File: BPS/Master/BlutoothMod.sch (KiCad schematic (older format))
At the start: 4 parts

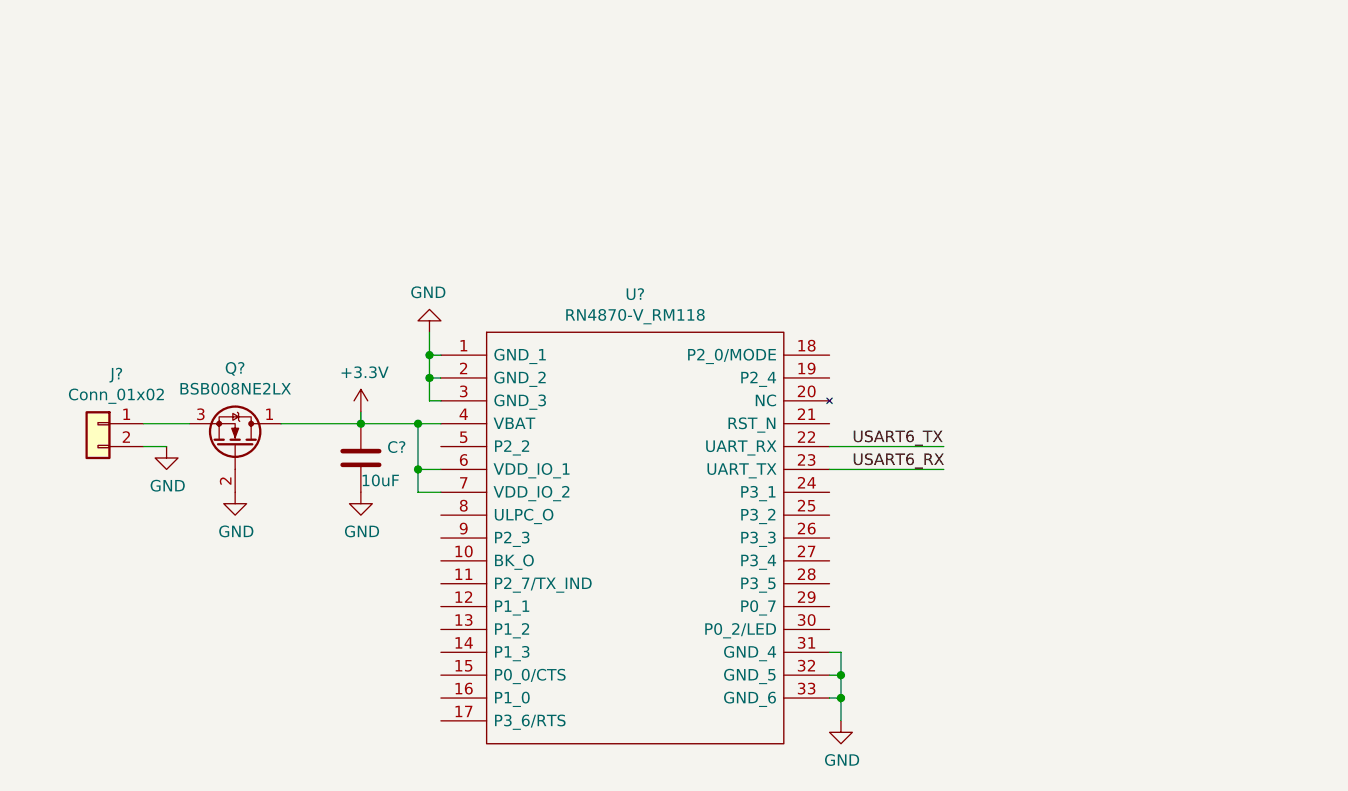
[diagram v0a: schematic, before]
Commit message: Added annotations to all schematic symbols. Ran electrical rules check. Need to figure out how to connect pins between sheets. Added reset circuit and finished reverse voltage protection circuit. Need to add configuration interface after finding out which pins to use on STM.
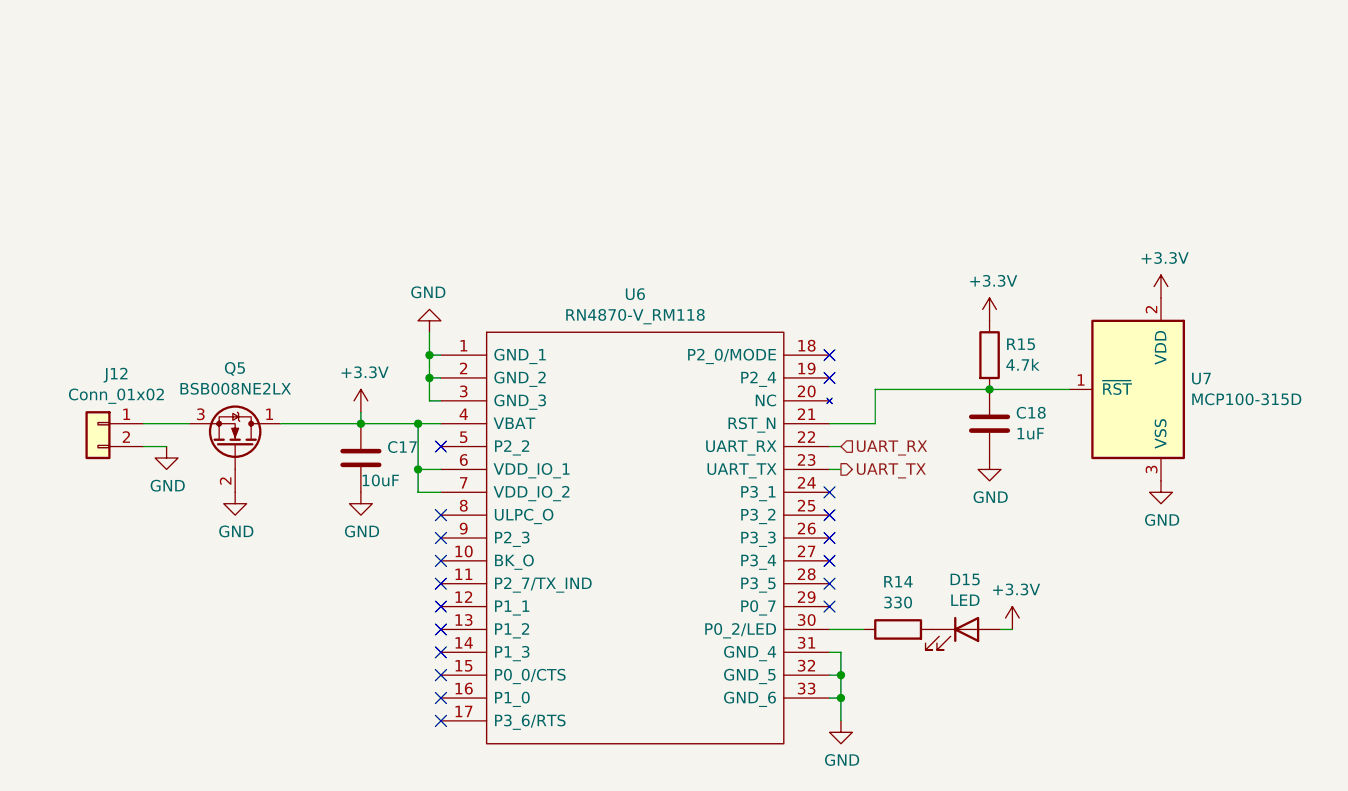
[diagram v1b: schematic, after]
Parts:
- added C18: 1uF, symbol Device:C
- added D15: LED, symbol Device:LED
- added R14: 330, symbol Device:R
- added R15: 4.7k, symbol Device:R
- added U7: MCP100-315D, symbol Power_Supervisor:MCP100-315D
- gave numbers to parts that had none: 4
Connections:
- net labels added: UART_RX, UART_TX
- net labels removed: USART6_RX, USART6_TX
- wire segments 24 -> 30
- no-connect marks 0 -> 19
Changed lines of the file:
@@
 $EndDescr
 $Comp
-L utsvt-bltmod:RN4870-V_RM118 U?
+L utsvt-bltmod:RN4870-V_RM118 U6
 U 1 1 5EE47912
 P 5000 2900
-F 0 "U?" H 5850 3165 50  0000 C CNN
+F 0 "U6" H 5850 3165 50  0000 C CNN
 F 1 "RN4870-V_RM118" H 5850 3074 50  0000 C CNN
 F 2 "RN4870IRM130" H 6550 3000 50  0001 L CNN
@@
 	1    0    0    -1
 $EndComp
-Text Label 6800 3300 0    50   ~ 0
-USART6_TX
-Wire Wire Line
-	6700 3300 7200 3300
-Wire Wire Line
-	6700 3400 7200 3400
-Text Label 6800 3400 0    50   ~ 0
-USART6_RX
 Wire Wire Line
 	6700 4200 6750 4200
@@
 Connection ~ 6750 4400
 $Comp
-L power:GND #PWR?
+L power:GND #PWR0106
 U 1 1 5EE48E9A
 P 6750 4500
-F 0 "#PWR?" H 6750 4250 50  0001 C CNN
+F 0 "#PWR0106" H 6750 4250 50  0001 C CNN
 F 1 "GND" H 6755 4327 50  0000 C CNN
 F 2 "" H 6750 4500 50  0001 C CNN
@@
 Connection ~ 4950 2900
 $Comp
-L power:GND #PWR?
+L power:GND #PWR0107
 U 1 1 5EE4937A
 P 4950 2800
-F 0 "#PWR?" H 4950 2550 50  0001 C CNN
+F 0 "#PWR0107" H 4950 2550 50  0001 C CNN
 F 1 "GND" H 4955 2627 50  0000 C CNN
 F 2 "" H 4950 2800 50  0001 C CNN
@@
 Connection ~ 4900 3200
 $Comp
-L power:GND #PWR?
+L power:GND #PWR0108
 U 1 1 5EE4ABF0
 P 4650 3500
-F 0 "#PWR?" H 4650 3250 50  0001 C CNN
+F 0 "#PWR0108" H 4650 3250 50  0001 C CNN
 F 1 "GND" H 4655 3327 50  0000 C CNN
 F 2 "" H 4650 3500 50  0001 C CNN
@@
 $EndComp
 $Comp
-L power:+3.3V #PWR?
+L power:+3.3V #PWR0109
 U 1 1 5EE4AD11
 P 4650 3150
-F 0 "#PWR?" H 4650 3000 50  0001 C CNN
+F 0 "#PWR0109" H 4650 3000 50  0001 C CNN
 F 1 "+3.3V" H 4665 3323 50  0000 C CNN
 F 2 "" H 4650 3150 50  0001 C CNN
@@
 $EndComp
 $Comp
-L Device:C C?
+L Device:C C17
 U 1 1 5EE4B59B
 P 4650 3350
-F 0 "C?" H 4765 3396 50  0000 L CNN
+F 0 "C17" H 4765 3396 50  0000 L CNN
 F 1 "10uF" H 4650 3250 50  0000 L CNN
 F 2 "" H 4688 3200 50  0001 C CNN
@@
 	4650 3200 4300 3200
 $Comp
-L Transistor_FET:BSB008NE2LX Q?
+L Transistor_FET:BSB008NE2LX Q5
 U 1 1 5EE62400
 P 4100 3300
-F 0 "Q?" V 4442 3300 50  0000 C CNN
+F 0 "Q5" V 4442 3300 50  0000 C CNN
 F 1 "BSB008NE2LX" V 4351 3300 50  0000 C CNN
 F 2 "Package_DirectFET:DirectFET_MX" H 4100 3300 50  0001 C CIN
@@
 $EndComp
 $Comp
-L power:GND #PWR?
+L power:GND #PWR0110
 U 1 1 5EE6457A
 P 4100 3500
-F 0 "#PWR?" H 4100 3250 50  0001 C CNN
+F 0 "#PWR0110" H 4100 3250 50  0001 C CNN
 F 1 "GND" H 4105 3327 50  0000 C CNN
 F 2 "" H 4100 3500 50  0001 C CNN
@@
 $EndComp
 $Comp
-L Connector_Generic:Conn_01x02 J?
+L Connector_Generic:Conn_01x02 J12
 U 1 1 5EE69056
 P 3500 3200
-F 0 "J?" H 3418 3417 50  0000 C CNN
+F 0 "J12" H 3418 3417 50  0000 C CNN
 F 1 "Conn_01x02" H 3418 3326 50  0000 C CNN
 F 2 "" H 3500 3200 50  0001 C CNN
@@
 	3700 3300 3800 3300
 $Comp
-L power:GND #PWR?
+L power:GND #PWR0111
 U 1 1 5EE6AECF
 P 3800 3300
-F 0 "#PWR?" H 3800 3050 50  0001 C CNN
+F 0 "#PWR0111" H 3800 3050 50  0001 C CNN
 F 1 "GND" H 3805 3127 50  0000 C CNN
 F 2 "" H 3800 3300 50  0001 C CNN
@@
 	1    0    0    -1
 $EndComp
+Wire Wire Line
+	6700 3200 6900 3200
+Wire Wire Line
+	6900 3200 6900 3050
+$Comp
+L Power_Supervisor:MCP100-315D U7
+U 1 1 5EE0F520
+P 8050 3050
+F 0 "U7" H 7820 3096 50  0000 R CNN
+F 1 "MCP100-315D" H 7820 3005 50  0000 R CNN
+F 2 "" H 7650 3200 50  0001 C CNN
+F 3 "http://ww1.microchip.com/downloads/en/DeviceDoc/11187f.pdf" H 7750 3300 50  0001 C CNN
+	1    8050 3050
+	-1   0    0    -1
+$EndComp
+Wire Wire Line
+	6900 3050 7400 3050
+$Comp
+L power:+3.3V #PWR0112
+U 1 1 5EE112CA
+P 7400 2750
+F 0 "#PWR0112" H 7400 2600 50  0001 C CNN
+F 1 "+3.3V" H 7415 2923 50  0000 C CNN
+F 2 "" H 7400 2750 50  0001 C CNN
+F 3 "" H 7400 2750 50  0001 C CNN
+	1    7400 2750
+	1    0    0    -1
+$EndComp
+$Comp
+L Device:R R15
+U 1 1 5EE108D1
+P 7400 2900
+F 0 "R15" H 7470 2946 50  0000 L CNN
+F 1 "4.7k" H 7470 2855 50  0000 L CNN
+F 2 "" V 7330 2900 50  0001 C CNN
+F 3 "~" H 7400 2900 50  0001 C CNN
+	1    7400 2900
+	1    0    0    -1
+$EndComp
+$Comp
+L Device:C C18
+U 1 1 5EE11D9D
+P 7400 3200
+F 0 "C18" H 7515 3246 50  0000 L CNN
+F 1 "1uF" H 7515 3155 50  0000 L CNN
+F 2 "" H 7438 3050 50  0001 C CNN
+F 3 "~" H 7400 3200 50  0001 C CNN
+	1    7400 3200
+	1    0    0    -1
+$EndComp
+Connection ~ 7400 3050
+$Comp
+L power:GND #PWR0113
+U 1 1 5EE12187
+P 7400 3350
+F 0 "#PWR0113" H 7400 3100 50  0001 C CNN
+F 1 "GND" H 7405 3177 50  0000 C CNN
+F 2 "" H 7400 3350 50  0001 C CNN
+F 3 "" H 7400 3350 50  0001 C CNN
+	1    7400 3350
+	1    0    0    -1
+$EndComp
+Wire Wire Line
+	7400 3050 7750 3050
+$Comp
+L power:GND #PWR0114
+U 1 1 5EE1353A
+P 8150 3450
+F 0 "#PWR0114" H 8150 3200 50  0001 C CNN
+F 1 "GND" H 8155 3277 50  0000 C CNN
+F 2 "" H 8150 3450 50  0001 C CNN
+F 3 "" H 8150 3450 50  0001 C CNN
+	1    8150 3450
+	1    0    0    -1
+$EndComp
+$Comp
+L power:+3.3V #PWR0115
+U 1 1 5EE13791
+P 8150 2650
+F 0 "#PWR0115" H 8150 2500 50  0001 C CNN
+F 1 "+3.3V" H 8165 2823 50  0000 C CNN
+F 2 "" H 8150 2650 50  0001 C CNN
+F 3 "" H 8150 2650 50  0001 C CNN
+	1    8150 2650
+	1    0    0    -1
+$EndComp
+$Comp
+L Device:R R14
+U 1 1 5EE13A0C
+P 7000 4100
+F 0 "R14" V 7207 4100 50  0000 C CNN
+F 1 "330" V 7116 4100 50  0000 C CNN
+F 2 "" V 6930 4100 50  0001 C CNN
+F 3 "~" H 7000 4100 50  0001 C CNN
+	1    7000 4100
+	0    -1   -1   0
+$EndComp
+Wire Wire Line
+	6700 4100 6850 4100
+$Comp
+L Device:LED D15
+U 1 1 5EE14D8D
+P 7300 4100
+F 0 "D15" H 7293 4317 50  0000 C CNN
+F 1 "LED" H 7293 4226 50  0000 C CNN
+F 2 "" H 7300 4100 50  0001 C CNN
+F 3 "~" H 7300 4100 50  0001 C CNN
+	1    7300 4100
+	1    0    0    -1
+$EndComp
+$Comp
+L power:+3.3V #PWR0116
+U 1 1 5EE14FBF
+P 7500 4100
+F 0 "#PWR0116" H 7500 3950 50  0001 C CNN
+F 1 "+3.3V" H 7515 4273 50  0000 C CNN
+F 2 "" H 7500 4100 50  0001 C CNN
+F 3 "" H 7500 4100 50  0001 C CNN
+	1    7500 4100
+	1    0    0    -1
+$EndComp
+Wire Wire Line
+	7450 4100 7500 4100
+NoConn ~ 6700 2900
+NoConn ~ 6700 3000
+NoConn ~ 6700 3500
+NoConn ~ 6700 3600
+NoConn ~ 6700 3700
+NoConn ~ 6700 3800
+NoConn ~ 6700 3900
+NoConn ~ 6700 4000
+NoConn ~ 5000 4500
+NoConn ~ 5000 4400
+NoConn ~ 5000 4300
+NoConn ~ 5000 4200
+NoConn ~ 5000 4100
+NoConn ~ 5000 4000
+NoConn ~ 5000 3900
+NoConn ~ 5000 3800
+NoConn ~ 5000 3700
+NoConn ~ 5000 3600
+NoConn ~ 5000 3300
+Text HLabel 6750 3300 2    50   Input ~ 0
+UART_RX
+Text HLabel 6750 3400 2    50   Output ~ 0
+UART_TX
+Wire Wire Line
+	6700 3300 6750 3300
+Wire Wire Line
+	6700 3400 6750 3400
 $EndSCHEMATC

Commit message: Connected hierarchial sheets. Added text for all status led's.
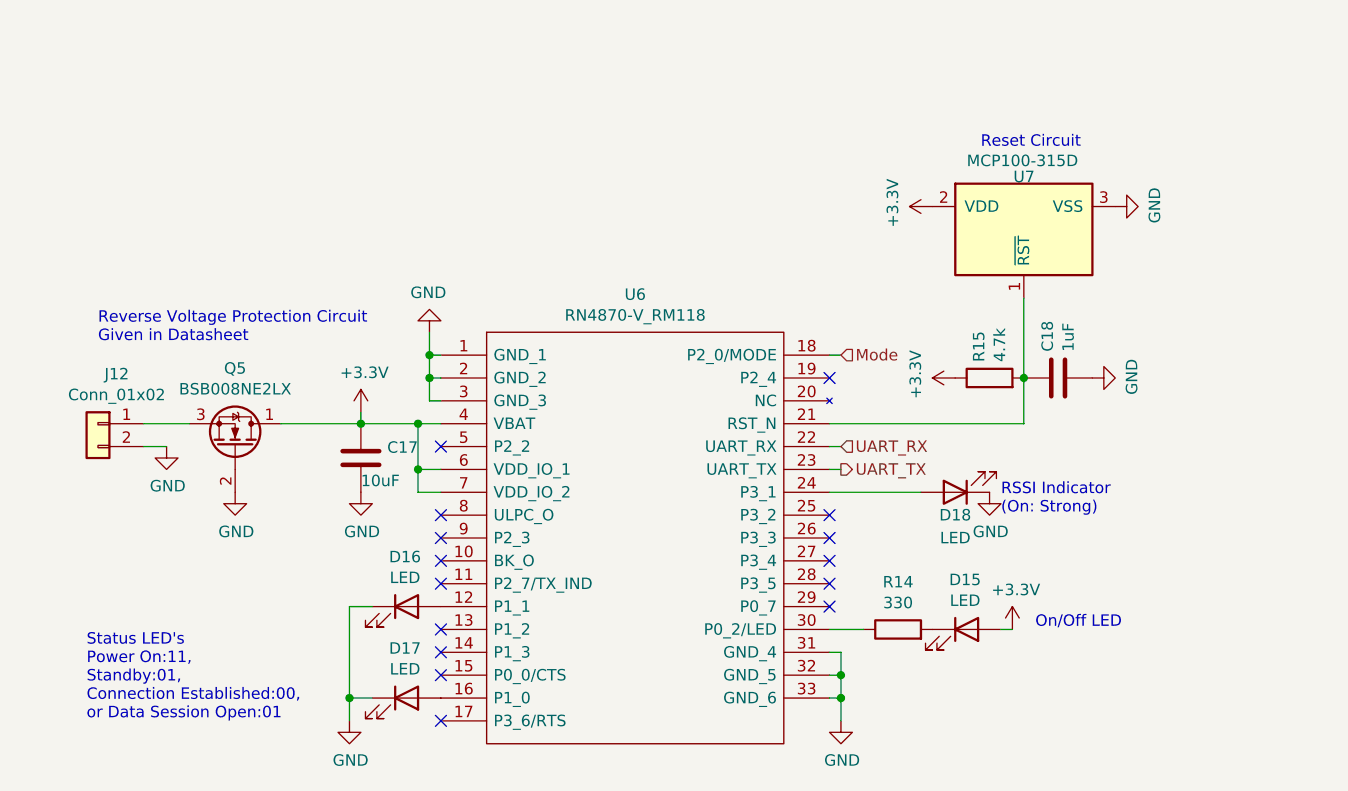
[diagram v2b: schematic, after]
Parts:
- added D16, D17, D18: LED, symbol Device:LED
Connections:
- net GND: now also D16.1 (K), D17.1 (K), D18.1 (K)
- net at U6.12 (P1_1): now also D16.2 (A)
- net at U6.16 (P1_0): now also D17.2 (A)
- net Mode: now reaches U6.18 (P2_0/MODE)
- net at U6.24 (P3_1): now also D18.2 (A)
- no-connect marks 19 -> 15
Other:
- note added: "On/Off LED"
- note added: "RSSI Indicator\n(On: Strong)"
- note added: "Reset Circuit\n"
- note added: "Reverse Voltage Protection Circuit\nGiven in Datasheet"
- note added: "Status LED's\nPower On:11,\nStandby:01,\nConnection Established:00,\nor Data Session Open:01"
- moved on the sheet: C18, R15, U7
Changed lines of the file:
@@
 	1    0    0    -1
 $EndComp
-Wire Wire Line
-	6700 3200 6900 3200
-Wire Wire Line
-	6900 3200 6900 3050
-$Comp
-L Power_Supervisor:MCP100-315D U7
-U 1 1 5EE0F520
-P 8050 3050
-F 0 "U7" H 7820 3096 50  0000 R CNN
-F 1 "MCP100-315D" H 7820 3005 50  0000 R CNN
-F 2 "" H 7650 3200 50  0001 C CNN
-F 3 "http://ww1.microchip.com/downloads/en/DeviceDoc/11187f.pdf" H 7750 3300 50  0001 C CNN
-	1    8050 3050
-	-1   0    0    -1
-$EndComp
-Wire Wire Line
-	6900 3050 7400 3050
 $Comp
 L power:+3.3V #PWR0112
 U 1 1 5EE112CA
-P 7400 2750
-F 0 "#PWR0112" H 7400 2600 50  0001 C CNN
-F 1 "+3.3V" H 7415 2923 50  0000 C CNN
-F 2 "" H 7400 2750 50  0001 C CNN
-F 3 "" H 7400 2750 50  0001 C CNN
-	1    7400 2750
-	1    0    0    -1
+P 7250 3000
+F 0 "#PWR0112" H 7250 2850 50  0001 C CNN
+F 1 "+3.3V" H 7265 3173 50  0000 C CNN
+F 2 "" H 7250 3000 50  0001 C CNN
+F 3 "" H 7250 3000 50  0001 C CNN
+	1    7250 3000
+	0    -1   -1   0
 $EndComp
 $Comp
 L Device:R R15
 U 1 1 5EE108D1
-P 7400 2900
-F 0 "R15" H 7470 2946 50  0000 L CNN
-F 1 "4.7k" H 7470 2855 50  0000 L CNN
-F 2 "" V 7330 2900 50  0001 C CNN
-F 3 "~" H 7400 2900 50  0001 C CNN
-	1    7400 2900
-	1    0    0    -1
+P 7400 3000
+F 0 "R15" H 7470 3046 50  0000 L CNN
+F 1 "4.7k" H 7470 2955 50  0000 L CNN
+F 2 "" V 7330 3000 50  0001 C CNN
+F 3 "~" H 7400 3000 50  0001 C CNN
+	1    7400 3000
+	0    -1   -1   0
 $EndComp
 $Comp
 L Device:C C18
 U 1 1 5EE11D9D
-P 7400 3200
-F 0 "C18" H 7515 3246 50  0000 L CNN
-F 1 "1uF" H 7515 3155 50  0000 L CNN
-F 2 "" H 7438 3050 50  0001 C CNN
-F 3 "~" H 7400 3200 50  0001 C CNN
-	1    7400 3200
-	1    0    0    -1
-$EndComp
-Connection ~ 7400 3050
+P 7700 3000
+F 0 "C18" H 7815 3046 50  0000 L CNN
+F 1 "1uF" H 7815 2955 50  0000 L CNN
+F 2 "" H 7738 2850 50  0001 C CNN
+F 3 "~" H 7700 3000 50  0001 C CNN
+	1    7700 3000
+	0    -1   -1   0
+$EndComp
+Connection ~ 7550 3000
 $Comp
 L power:GND #PWR0113
 U 1 1 5EE12187
-P 7400 3350
-F 0 "#PWR0113" H 7400 3100 50  0001 C CNN
-F 1 "GND" H 7405 3177 50  0000 C CNN
-F 2 "" H 7400 3350 50  0001 C CNN
-F 3 "" H 7400 3350 50  0001 C CNN
-	1    7400 3350
-	1    0    0    -1
-$EndComp
-Wire Wire Line
-	7400 3050 7750 3050
+P 7850 3000
+F 0 "#PWR0113" H 7850 2750 50  0001 C CNN
+F 1 "GND" H 7855 2827 50  0000 C CNN
+F 2 "" H 7850 3000 50  0001 C CNN
+F 3 "" H 7850 3000 50  0001 C CNN
+	1    7850 3000
+	0    -1   -1   0
+$EndComp
+Wire Wire Line
+	7550 3000 7550 2650
 $Comp
 L power:GND #PWR0114
 U 1 1 5EE1353A
-P 8150 3450
-F 0 "#PWR0114" H 8150 3200 50  0001 C CNN
-F 1 "GND" H 8155 3277 50  0000 C CNN
-F 2 "" H 8150 3450 50  0001 C CNN
-F 3 "" H 8150 3450 50  0001 C CNN
-	1    8150 3450
-	1    0    0    -1
+P 7950 2250
+F 0 "#PWR0114" H 7950 2000 50  0001 C CNN
+F 1 "GND" H 7955 2077 50  0000 C CNN
+F 2 "" H 7950 2250 50  0001 C CNN
+F 3 "" H 7950 2250 50  0001 C CNN
+	1    7950 2250
+	0    -1   -1   0
 $EndComp
 $Comp
 L power:+3.3V #PWR0115
 U 1 1 5EE13791
-P 8150 2650
-F 0 "#PWR0115" H 8150 2500 50  0001 C CNN
-F 1 "+3.3V" H 8165 2823 50  0000 C CNN
-F 2 "" H 8150 2650 50  0001 C CNN
-F 3 "" H 8150 2650 50  0001 C CNN
-	1    8150 2650
-	1    0    0    -1
+P 7150 2250
+F 0 "#PWR0115" H 7150 2100 50  0001 C CNN
+F 1 "+3.3V" H 7165 2423 50  0000 C CNN
+F 2 "" H 7150 2250 50  0001 C CNN
+F 3 "" H 7150 2250 50  0001 C CNN
+	1    7150 2250
+	0    -1   -1   0
 $EndComp
 $Comp
@@
 Wire Wire Line
 	7450 4100 7500 4100
-NoConn ~ 6700 2900
 NoConn ~ 6700 3000
-NoConn ~ 6700 3500
 NoConn ~ 6700 3600
 NoConn ~ 6700 3700
@@
 NoConn ~ 6700 4000
 NoConn ~ 5000 4500
-NoConn ~ 5000 4400
 NoConn ~ 5000 4300
 NoConn ~ 5000 4200
 NoConn ~ 5000 4100
-NoConn ~ 5000 4000
 NoConn ~ 5000 3900
 NoConn ~ 5000 3800
@@
 Text HLabel 6750 3400 2    50   Output ~ 0
 UART_TX
+$Comp
+L Device:LED D16
+U 1 1 5EE20E59
+P 4850 4000
+F 0 "D16" H 4843 4217 50  0000 C CNN
+F 1 "LED" H 4843 4126 50  0000 C CNN
+F 2 "" H 4850 4000 50  0001 C CNN
+F 3 "~" H 4850 4000 50  0001 C CNN
+	1    4850 4000
+	1    0    0    -1
+$EndComp
+$Comp
+L Device:LED D17
+U 1 1 5EE21939
+P 4850 4400
+F 0 "D17" H 4843 4617 50  0000 C CNN
+F 1 "LED" H 4843 4526 50  0000 C CNN
+F 2 "" H 4850 4400 50  0001 C CNN
+F 3 "~" H 4850 4400 50  0001 C CNN
+	1    4850 4400
+	1    0    0    -1
+$EndComp
+Wire Wire Line
+	4700 4000 4600 4000
+Wire Wire Line
+	4600 4000 4600 4400
+Wire Wire Line
+	4600 4400 4700 4400
+Wire Wire Line
+	4600 4400 4600 4500
+Connection ~ 4600 4400
+$Comp
+L power:GND #PWR0117
+U 1 1 5EE2468E
+P 4600 4500
+F 0 "#PWR0117" H 4600 4250 50  0001 C CNN
+F 1 "GND" H 4605 4327 50  0000 C CNN
+F 2 "" H 4600 4500 50  0001 C CNN
+F 3 "" H 4600 4500 50  0001 C CNN
+	1    4600 4500
+	1    0    0    -1
+$EndComp
+Text HLabel 6750 2900 2    50   Input ~ 0
+Mode
+Text Notes 3500 2850 0    50   ~ 0
+Reverse Voltage Protection Circuit\nGiven in Datasheet
+Text Notes 3450 4500 0    50   ~ 0
+Status LED's\nPower On:11,\nStandby:01,\nConnection Established:00,\nor Data Session Open:01
+Text Notes 7600 4100 0    50   ~ 0
+On/Off LED
+Text Notes 7800 2000 2    50   ~ 0
+Reset Circuit\n
 Wire Wire Line
 	6700 3300 6750 3300
 Wire Wire Line
 	6700 3400 6750 3400
+Wire Wire Line
+	6700 2900 6750 2900
+$Comp
+L Power_Supervisor:MCP100-315D U7
+U 1 1 5EE0F520
+P 7550 2350
+F 0 "U7" V 7320 2396 50  0000 R CNN
+F 1 "MCP100-315D" V 7250 2600 50  0000 R CNN
+F 2 "" H 7150 2500 50  0001 C CNN
+F 3 "http://ww1.microchip.com/downloads/en/DeviceDoc/11187f.pdf" H 7250 2600 50  0001 C CNN
+	1    7550 2350
+	0    -1   1    0
+$EndComp
+Wire Wire Line
+	6700 3200 7550 3200
+Wire Wire Line
+	7550 3200 7550 3000
+$Comp
+L Device:LED D18
+U 1 1 5EE54DD1
+P 7250 3500
+F 0 "D18" H 7250 3600 50  0000 C CNN
+F 1 "LED" H 7250 3700 50  0000 C CNN
+F 2 "" H 7250 3500 50  0001 C CNN
+F 3 "~" H 7250 3500 50  0001 C CNN
+	1    7250 3500
+	-1   0    0    1
+$EndComp
+$Comp
+L power:GND #PWR033
+U 1 1 5EE552B9
+P 7400 3500
+F 0 "#PWR033" H 7400 3250 50  0001 C CNN
+F 1 "GND" H 7405 3327 50  0000 C CNN
+F 2 "" H 7400 3500 50  0001 C CNN
+F 3 "" H 7400 3500 50  0001 C CNN
+	1    7400 3500
+	1    0    0    -1
+$EndComp
+Wire Wire Line
+	6700 3500 7100 3500
+Text Notes 7450 3600 0    50   ~ 0
+RSSI Indicator\n(On: Strong)
 $EndSCHEMATC
